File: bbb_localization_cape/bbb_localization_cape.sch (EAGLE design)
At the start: 31 parts, among them J2 MOLEX-22-03-5035, U1 SN65HVD256DR, U2 ARDUCAMOV5642, U3 SN74LV1T126DCKR, U4 MSP430G2553IPW20R, U5 SN74LV1T125DCKR, U6 LP38693MP-3.3/NOPB, U7 LM1085ISX-ADJ, U8 SN74LV1T126DCKR

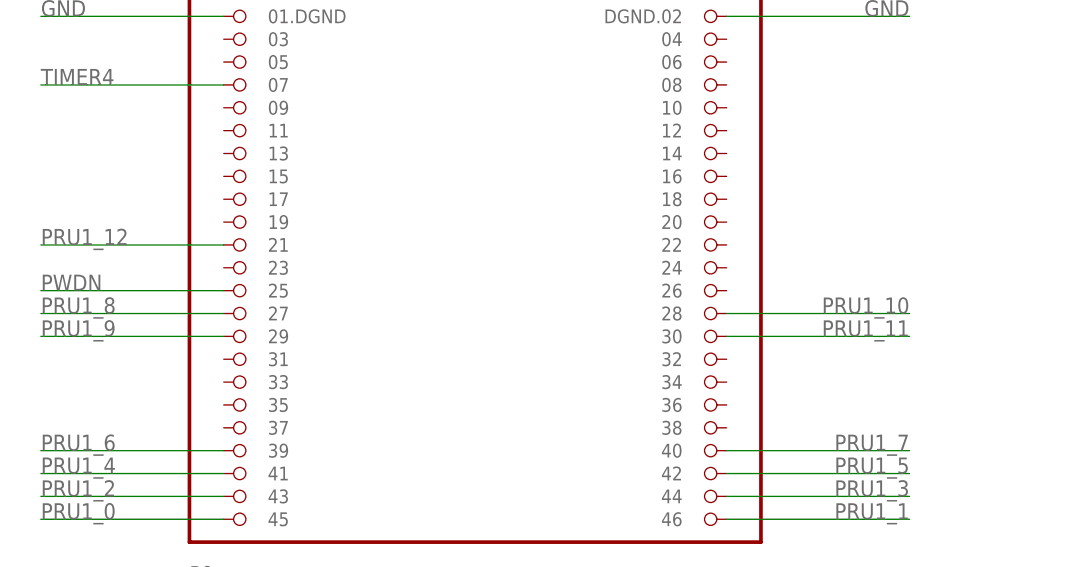
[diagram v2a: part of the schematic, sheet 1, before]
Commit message: Passing ERC, still need to go through DRC
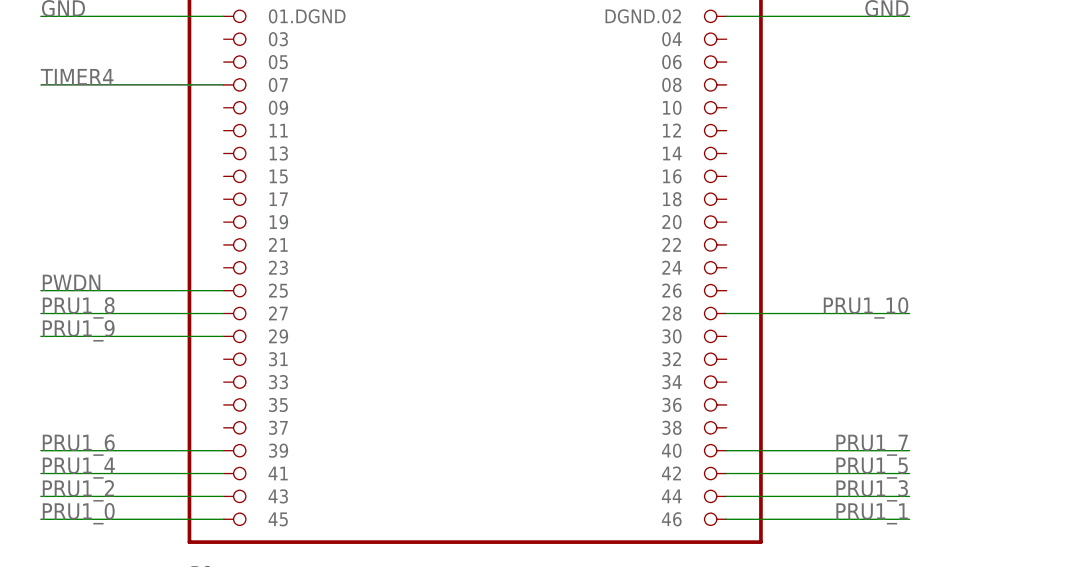
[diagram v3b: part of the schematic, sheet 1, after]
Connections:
- removed net PRU1_11: A1.30@P8
- removed net PRU1_12: A1.21@P8
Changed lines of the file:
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@@
 <grid distance="0.1" unitdist="inch" unit="inch" style="lines" multiple="1" display="no" altdistance="0.01" altunitdist="inch" altunit="inch"/>
 <layers>
-<layer number="1" name="Top" color="4" fill="1" visible="yes" active="no"/>
-<layer number="2" name="Route2" color="1" fill="3" visible="yes" active="no"/>
-<layer number="3" name="Route3" color="4" fill="3" visible="yes" active="no"/>
-<layer number="4" name="Route4" color="1" fill="4" visible="yes" active="no"/>
-<layer number="5" name="Route5" color="4" fill="4" visible="yes" active="no"/>
-<layer number="6" name="Route6" color="1" fill="8" visible="yes" active="no"/>
-<layer number="7" name="Route7" color="4" fill="8" visible="yes" active="no"/>
-<layer number="8" name="Route8" color="1" fill="2" visible="yes" active="no"/>
-<layer number="9" name="Route9" color="4" fill="2" visible="yes" active="no"/>
-<layer number="10" name="Route10" color="1" fill="7" visible="yes" active="no"/>
-<layer number="11" name="Route11" color="4" fill="7" visible="yes" active="no"/>
-<layer number="12" name="Route12" color="1" fill="5" visible="yes" active="no"/>
-<layer number="13" name="Route13" color="4" fill="5" visible="yes" active="no"/>
-<layer number="14" name="Route14" color="1" fill="6" visible="yes" active="no"/>
-<layer number="15" name="Route15" color="4" fill="6" visible="yes" active="no"/>
-<layer number="16" name="Bottom" color="1" fill="1" visible="yes" active="no"/>
-<layer number="17" name="Pads" color="2" fill="1" visible="yes" active="no"/>
-<layer number="18" name="Vias" color="2" fill="1" visible="yes" active="no"/>
-<layer number="19" name="Unrouted" color="6" fill="1" visible="yes" active="no"/>
-<layer number="20" name="Dimension" color="24" fill="1" visible="yes" active="no"/>
-<layer number="21" name="tPlace" color="7" fill="1" visible="yes" active="no"/>
-<layer number="22" name="bPlace" color="7" fill="1" visible="yes" active="no"/>
-<layer number="23" name="tOrigins" color="15" fill="1" visible="yes" active="no"/>
-<layer number="24" name="bOrigins" color="15" fill="1" visible="yes" active="no"/>
-<layer number="25" name="tNames" color="7" fill="1" visible="yes" active="no"/>
-<layer number="26" name="bNames" color="7" fill="1" visible="yes" active="no"/>
-<layer number="27" name="tValues" color="7" fill="1" visible="yes" active="no"/>
-<layer number="28" name="bValues" color="7" fill="1" visible="yes" active="no"/>
+<layer number="1" name="Top" color="4" fill="1" visible="no" active="no"/>
+<layer number="2" name="Route2" color="1" fill="3" visible="no" active="no"/>
+<layer number="3" name="Route3" color="4" fill="3" visible="no" active="no"/>
+<layer number="4" name="Route4" color="1" fill="4" visible="no" active="no"/>
+<layer number="5" name="Route5" color="4" fill="4" visible="no" active="no"/>
+<layer number="6" name="Route6" color="1" fill="8" visible="no" active="no"/>
+<layer number="7" name="Route7" color="4" fill="8" visible="no" active="no"/>
+<layer number="8" name="Route8" color="1" fill="2" visible="no" active="no"/>
+<layer number="9" name="Route9" color="4" fill="2" visible="no" active="no"/>
+<layer number="10" name="Route10" color="1" fill="7" visible="no" active="no"/>
+<layer number="11" name="Route11" color="4" fill="7" visible="no" active="no"/>
+<layer number="12" name="Route12" color="1" fill="5" visible="no" active="no"/>
+<layer number="13" name="Route13" color="4" fill="5" visible="no" active="no"/>
+<layer number="14" name="Route14" color="1" fill="6" visible="no" active="no"/>
+<layer number="15" name="Route15" color="4" fill="6" visible="no" active="no"/>
+<layer number="16" name="Bottom" color="1" fill="1" visible="no" active="no"/>
+<layer number="17" name="Pads" color="2" fill="1" visible="no" active="no"/>
+<layer number="18" name="Vias" color="2" fill="1" visible="no" active="no"/>
+<layer number="19" name="Unrouted" color="6" fill="1" visible="no" active="no"/>
+<layer number="20" name="Dimension" color="24" fill="1" visible="no" active="no"/>
+<layer number="21" name="tPlace" color="7" fill="1" visible="no" active="no"/>
+<layer number="22" name="bPlace" color="7" fill="1" visible="no" active="no"/>
+<layer number="23" name="tOrigins" color="15" fill="1" visible="no" active="no"/>
+<layer number="24" name="bOrigins" color="15" fill="1" visible="no" active="no"/>
+<layer number="25" name="tNames" color="7" fill="1" visible="no" active="no"/>
+<layer number="26" name="bNames" color="7" fill="1" visible="no" active="no"/>
+<layer number="27" name="tValues" color="7" fill="1" visible="no" active="no"/>
+<layer number="28" name="bValues" color="7" fill="1" visible="no" active="no"/>
 <layer number="29" name="tStop" color="7" fill="3" visible="no" active="no"/>
 <layer number="30" name="bStop" color="7" fill="6" visible="no" active="no"/>
@@
 <layer number="35" name="tGlue" color="7" fill="4" visible="no" active="no"/>
 <layer number="36" name="bGlue" color="7" fill="5" visible="no" active="no"/>
-<layer number="37" name="tTest" color="7" fill="1" visible="yes" active="no"/>
-<layer number="38" name="bTest" color="7" fill="1" visible="yes" active="no"/>
+<layer number="37" name="tTest" color="7" fill="1" visible="no" active="no"/>
+<layer number="38" name="bTest" color="7" fill="1" visible="no" active="no"/>
 <layer number="39" name="tKeepout" color="4" fill="11" visible="no" active="no"/>
 <layer number="40" name="bKeepout" color="1" fill="11" visible="no" active="no"/>
@@
 <layer number="44" name="Drills" color="7" fill="1" visible="no" active="no"/>
 <layer number="45" name="Holes" color="7" fill="1" visible="no" active="no"/>
-<layer number="46" name="Milling" color="3" fill="1" visible="yes" active="no"/>
-<layer number="47" name="Measures" color="7" fill="1" visible="yes" active="no"/>
-<layer number="48" name="Document" color="7" fill="1" visible="yes" active="no"/>
-<layer number="49" name="Reference" color="7" fill="1" visible="yes" active="no"/>
-<layer number="50" name="dxf" color="7" fill="1" visible="yes" active="no"/>
-<layer number="51" name="tDocu" color="7" fill="1" visible="yes" active="no"/>
-<layer number="52" name="bDocu" color="7" fill="1" visible="yes" active="no"/>
-<layer number="53" name="tGND_GNDA" color="7" fill="9" visible="yes" active="no"/>
-<layer number="54" name="bGND_GNDA" color="1" fill="9" visible="yes" active="no"/>
-<layer number="56" name="wert" color="7" fill="1" visible="yes" active="no"/>
-<layer number="57" name="tCAD" color="7" fill="1" visible="yes" active="no"/>
-<layer number="59" name="tCarbon" color="7" fill="1" visible="yes" active="no"/>
-<layer number="60" name="bCarbon" color="7" fill="1" visible="yes" active="no"/>
+<layer number="46" name="Milling" color="3" fill="1" visible="no" active="no"/>
+<layer number="47" name="Measures" color="7" fill="1" visible="no" active="no"/>
+<layer number="48" name="Document" color="7" fill="1" visible="no" active="no"/>
+<layer number="49" name="Reference" color="7" fill="1" visible="no" active="no"/>
+<layer number="50" name="dxf" color="7" fill="1" visible="no" active="no"/>
+<layer number="51" name="tDocu" color="7" fill="1" visible="no" active="no"/>
+<layer number="52" name="bDocu" color="7" fill="1" visible="no" active="no"/>
+<layer number="53" name="tGND_GNDA" color="7" fill="9" visible="no" active="no"/>
+<layer number="54" name="bGND_GNDA" color="1" fill="9" visible="no" active="no"/>
+<layer number="56" name="wert" color="7" fill="1" visible="no" active="no"/>
+<layer number="57" name="tCAD" color="7" fill="1" visible="no" active="no"/>
+<layer number="59" name="tCarbon" color="7" fill="1" visible="no" active="no"/>
+<layer number="60" name="bCarbon" color="7" fill="1" visible="no" active="no"/>
 <layer number="90" name="Modules" color="5" fill="1" visible="yes" active="yes"/>
 <layer number="91" name="Nets" color="2" fill="1" visible="yes" active="yes"/>
@@
 </segment>
 </net>
-<net name="PRU1_11" class="1">
-<segment>
-<pinref part="A1" gate="G$1" pin="30@P8"/>
-<wire x1="109.22" y1="152.4" x2="129.54" y2="152.4" width="0.1524" layer="91"/>
-<label x="129.54" y="152.4" size="1.778" layer="95" rot="MR0"/>
-</segment>
-</net>
 <net name="PRU1_10" class="1">
 <segment>
@@
 </segment>
 </net>
-<net name="PRU1_12" class="1">
-<segment>
-<pinref part="A1" gate="G$1" pin="21@P8"/>
-<wire x1="53.34" y1="162.56" x2="33.02" y2="162.56" width="0.1524" layer="91"/>
-<label x="33.02" y="162.56" size="1.778" layer="95"/>
-</segment>
-</net>

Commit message: Labeled everything
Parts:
- removed C8: 4.7uF, resistor:C-USC0805
- removed R7: 910, resistor:R-US_R0805
- added C1: 100nF, resistor:C-USC0805
- added R3: 10k, resistor:R-US_R0805
- C2: value 100nF -> 10uF; device resistor:C-USC0805 -> resistor:C-USC1206
- C4: value 10uF -> 22uF; device resistor:C-USC1206 -> resistor:C-USC0805
- C5: value 22uF -> 1uF
- C7: value 1uF -> 4.7uF
- R4: value 10k -> 47k
- R5: value 47k -> 130
- R6: value 130 -> 910
- U3: value SN74LV1T126DCKR -> MSP430G2553IPW20R; device bbb_localization_cape:SN74LV1T126DCKR -> bbb_cape_parts:MSP430G2553IPW20R
- U4: value MSP430G2553IPW20R -> SN74LV1T126DCKR; device bbb_cape_parts:MSP430G2553IPW20R -> bbb_localization_cape:SN74LV1T126DCKR
- U6: value LP38693MP-3.3/NOPB -> SN74LV1T126DCKR; device bbb_localization_cape:LP38693MP-3.3/NOPB -> bbb_localization_cape:SN74LV1T126DCKR
- U7: value LM1085ISX-ADJ -> LP38693MP-3.3/NOPB; device bbb_localization_cape:LM1085ISX-ADJ -> bbb_localization_cape:LP38693MP-3.3/NOPB
- U8: value SN74LV1T126DCKR -> LM1085ISX-ADJ; device bbb_localization_cape:SN74LV1T126DCKR -> bbb_localization_cape:LM1085ISX-ADJ
- renumbered +12V to PAD1, C9 to C6, GND to PAD2
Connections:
- net +10V: now also R5.2, U8.OUT, U8.TAB; no longer R6.2, U7.OUT, U7.TAB
- net +12V: now also C2.1, U8.IN; no longer C4.1, U7.IN
- net +3V3: now also C7.1, R4.2, U3.DVCC, U7.VOUT; no longer C8.1, R5.2, U4.DVCC, U6.VOUT
- net +5V: now also C4.1, U4.VCC, U6.OE, U6.VCC, U7.VIN; no longer C7.1, U3.VCC, U6.VIN, U8.OE, U8.VCC
- net DATA_DYN: now also R3.1, U4.Y; no longer R4.1, U3.Y
- net GND: now also C1.2, R6.1, U3.DVSS, U4.GND, U7.GND; no longer C8.2, R7.1, U3.GND, U4.DVSS, U8.GND
- net I2C2_SCL: now also U3.P1.6/TA0.1/UCB0SOMI/UCB0SCL/A6/CA6/TDI/TCLK; no longer U4.P1.6/TA0.1/UCB0SOMI/UCB0SCL/A6/CA6/TDI/TCLK
- net I2C2_SDA: now also U3.P1.7/CAOUT/UCB0SIMO/UCB0SDA/A7/CA7/TDO/TDI; no longer U4.P1.7/CAOUT/UCB0SIMO/UCB0SDA/A7/CA7/TDO/TDI
- net N$3: now also R5.1, R6.2, U8.ADJ; no longer R6.1, R7.2, U7.ADJ
- net RST: now also C1.1, R4.1, U3.!RST/NMI/SBWTDIO; no longer C2.1, R5.1, U4.!RST/NMI/SBWTDIO
- net SYS_RESETN: now also U6.A; no longer U8.A
- net SYS_RESETN_5V: now also R3.2, U6.Y, U7.VEN; no longer R4.2, U6.VEN, U8.Y
- net TEST: now also U3.TEST/SBWTCK; no longer U4.TEST/SBWTCK
- net UART2_DIR: now also SJ2.3; no longer SJ1.3
- net UART2_TXD: now also SJ1.3; no longer SJ2.3
- net UART_DYN_DIR: now also SJ2.2, U4.OE; no longer SJ1.2, U3.OE
- net UART_DYN_TXD: now also SJ1.2, U4.A; no longer SJ2.2, U3.A
- net UART_MSP_DIR: now also SJ2.1, U3.P2.0/TA1.0; no longer SJ1.1, U4.P2.0/TA1.0
- net UART_MSP_RXD: now also U3.P1.1/TA0.0/UCA0RXD/UCA0SOMI/A1/CA1; no longer U4.P1.1/TA0.0/UCA0RXD/UCA0SOMI/A1/CA1
- net UART_MSP_TXD: now also SJ1.1, U3.P1.2/TA0.1/UCA0TXD/UCA0SIMO/A2/CA2; no longer SJ2.1, U4.P1.2/TA0.1/UCA0TXD/UCA0SIMO/A2/CA2
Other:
- moved on the sheet: C4, C5, C7, R4, R6, U6

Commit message: Done, needs external review
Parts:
- C2: device resistor:C-USC1206 -> resistor:C-USC0805
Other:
- moved on the sheet: C3, PS1
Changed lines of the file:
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@@
 <part name="P+8" library="supply1" library_urn="urn:adsk.eagle:library:371" deviceset="+5V" device=""/>
 <part name="+3V38" library="supply1" library_urn="urn:adsk.eagle:library:371" deviceset="+3V3" device=""/>
-<part name="C2" library="resistor" library_urn="urn:adsk.eagle:library:348" deviceset="C-US" device="C1206" package3d_urn="urn:adsk.eagle:package:26140/1" value="10uF"/>
+<part name="C2" library="resistor" library_urn="urn:adsk.eagle:library:348" deviceset="C-US" device="C0805" package3d_urn="urn:adsk.eagle:package:26137/1" value="10uF"/>
 <part name="C4" library="resistor" library_urn="urn:adsk.eagle:library:348" deviceset="C-US" device="C0805" package3d_urn="urn:adsk.eagle:package:26137/1" value="22uF"/>
 <part name="C6" library="resistor" library_urn="urn:adsk.eagle:library:348" deviceset="C-US" device="C1210" package3d_urn="urn:adsk.eagle:package:26139/1" value="100uF"/>
@@
 <instance part="SUPPLY3" gate="G$1" x="226.06" y="104.14"/>
 <instance part="PS1" gate="A" x="73.66" y="76.2"/>
-<instance part="P+5" gate="1" x="50.8" y="81.28" smashed="yes">
-<attribute name="VALUE" x="50.8" y="81.28" size="1.778" layer="96"/>
+<instance part="P+5" gate="1" x="45.72" y="81.28" smashed="yes">
+<attribute name="VALUE" x="48.26" y="81.28" size="1.778" layer="96"/>
 </instance>
 <instance part="P+6" gate="1" x="96.52" y="81.28" smashed="yes">
@@
 <instance part="C4" gate="G$1" x="96.52" y="66.04"/>
 <instance part="C6" gate="G$1" x="226.06" y="83.82"/>
-<instance part="C3" gate="G$1" x="50.8" y="66.04"/>
+<instance part="C3" gate="G$1" x="45.72" y="66.04"/>
 <instance part="GND9" gate="1" x="96.52" y="50.8"/>
 <instance part="FRAME3" gate="G$1" x="0" y="0"/>
@@
 <segment>
 <pinref part="PS1" gate="A" pin="GND"/>
-<wire x1="73.66" y1="66.04" x2="73.66" y2="55.88" width="0.1524" layer="91"/>
-<wire x1="96.52" y1="55.88" x2="73.66" y2="55.88" width="0.1524" layer="91"/>
+<wire x1="55.88" y1="73.66" x2="55.88" y2="55.88" width="0.1524" layer="91"/>
+<wire x1="96.52" y1="55.88" x2="55.88" y2="55.88" width="0.1524" layer="91"/>
 <pinref part="C4" gate="G$1" pin="2"/>
 <wire x1="96.52" y1="60.96" x2="96.52" y2="55.88" width="0.1524" layer="91"/>
 <pinref part="C3" gate="G$1" pin="2"/>
-<wire x1="50.8" y1="60.96" x2="50.8" y2="55.88" width="0.1524" layer="91"/>
-<wire x1="50.8" y1="55.88" x2="73.66" y2="55.88" width="0.1524" layer="91"/>
-<junction x="73.66" y="55.88"/>
+<wire x1="45.72" y1="60.96" x2="45.72" y2="55.88" width="0.1524" layer="91"/>
+<wire x1="45.72" y1="55.88" x2="55.88" y2="55.88" width="0.1524" layer="91"/>
+<junction x="55.88" y="55.88"/>
 <pinref part="GND9" gate="1" pin="GND"/>
 <wire x1="96.52" y1="53.34" x2="96.52" y2="55.88" width="0.1524" layer="91"/>
@@
 <pinref part="PS1" gate="A" pin="VIN"/>
 <pinref part="P+5" gate="1" pin="+12V"/>
-<wire x1="55.88" y1="76.2" x2="50.8" y2="76.2" width="0.1524" layer="91"/>
-<wire x1="50.8" y1="76.2" x2="50.8" y2="78.74" width="0.1524" layer="91"/>
+<wire x1="55.88" y1="76.2" x2="45.72" y2="76.2" width="0.1524" layer="91"/>
+<wire x1="45.72" y1="76.2" x2="45.72" y2="78.74" width="0.1524" layer="91"/>
 <pinref part="C3" gate="G$1" pin="1"/>
-<wire x1="50.8" y1="68.58" x2="50.8" y2="76.2" width="0.1524" layer="91"/>
-<junction x="50.8" y="76.2"/>
-</segment>
-</net>
+<wire x1="45.72" y1="68.58" x2="45.72" y2="76.2" width="0.1524" layer="91"/>
+<junction x="45.72" y="76.2"/>
+</segment>
+</net>

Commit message: Began adding 3D models of components
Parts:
- R1, R2, R3, R4, R5, R6: device resistor:R-US_R0805 -> rcl:R-US_R0805
- U3: device bbb_cape_parts:MSP430G2553IPW20R -> bbb_localization_cape:MSP430G2553IPW20R
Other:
- note added: "1.0"
- note added: "Cape Header, ArduCam, UART, CAN"
- note added: "DC/DC Converters"
- note added: "MSP, Half-Duplex UART"
